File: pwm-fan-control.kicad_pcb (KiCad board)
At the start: 2 copper layers, 29 x 20.5 mm, 20 parts, among them J1 Fan-out, J2 PWM and power, J4 Fan-out, Q1 Q_PMOS_GSD, Q2 Q_PMOS_GSD, U1 LM358

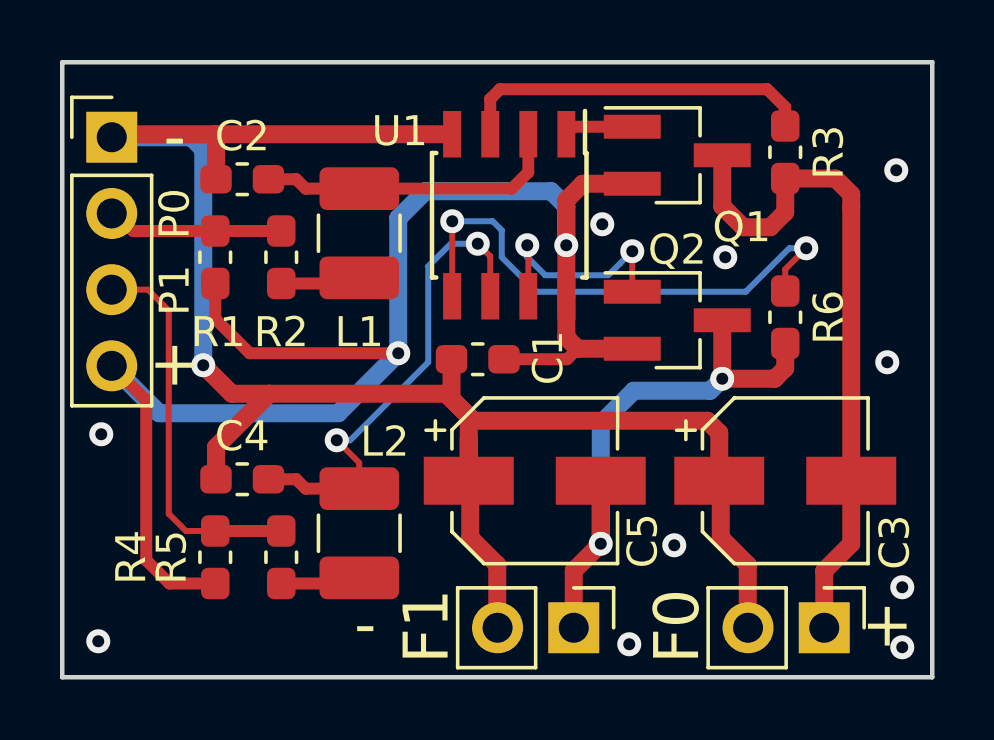
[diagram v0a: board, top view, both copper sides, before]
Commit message: improved bird, added silscreen to the back
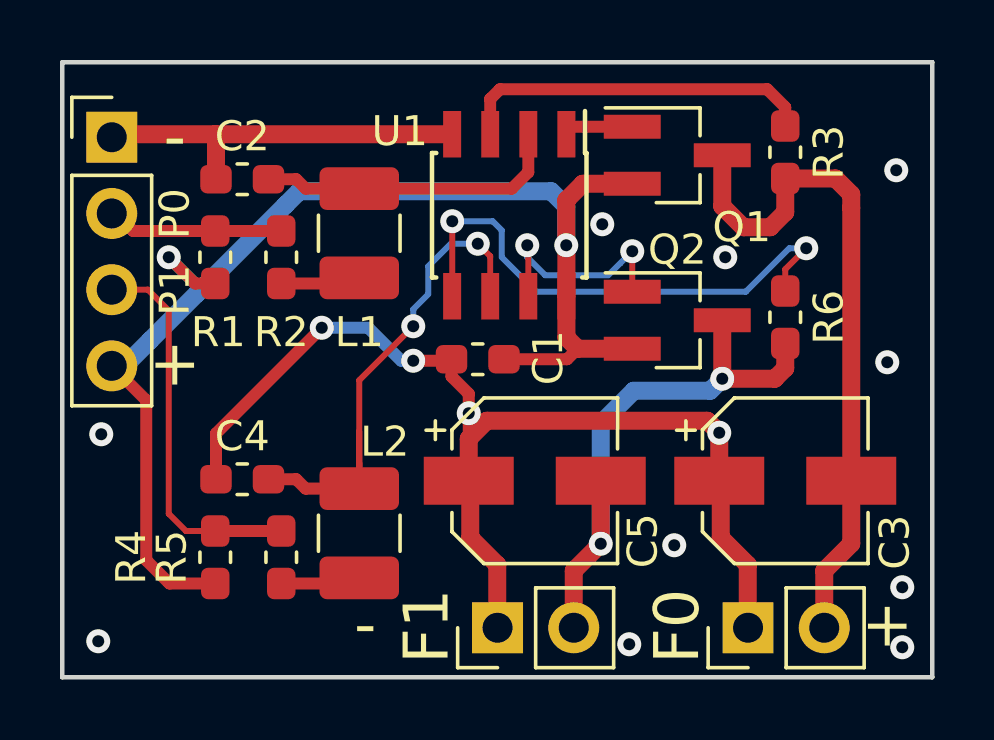
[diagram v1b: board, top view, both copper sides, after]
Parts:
- removed the G*** at (135.7, 56.7)
- added G***: LOGO, graphics:kiwi, B.Cu at (139.0, 55.5)
- moved J4 2.54 mm to (145.5, 58.9), turned to 90 degrees
- moved J1 2.54 mm to (153.9, 58.9), turned to 90 degrees
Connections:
- J1 pad 1: /VFAN0 -> GND
- J1 pad 2: GND -> /VFAN0
- J4 pad 1: /VFAN1 -> GND
- J4 pad 2: GND -> /VFAN1
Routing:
- net GND: track 64.6 -> 50.9 mm, vias 11 -> 14
- net VCCFan: track 54.7 -> 43.4 mm
- net Net-(C4-Pad2): track 16.3 -> 18.2 mm

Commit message: Updated gerbers
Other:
- board text added: "FAN0"
- board text added: "FAN1"
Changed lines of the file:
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@@
   (general
     (thickness 1.6)
-    (drawings 17)
+    (drawings 23)
     (tracks 162)
     (zones 0)
@@
       (xy 1.961326 4.735749) (xy 2.887919 4.58736)) (layer B.Mask) (width 0.01))
   )
+  (gr_text + (at 148 54.4) (layer B.SilkS)
+    (effects (font (size 1.5 1.5) (thickness 0.3)) (justify mirror))
+  )
+  (gr_text + (at 156.4 54.4) (layer B.SilkS)
+    (effects (font (size 1.5 1.5) (thickness 0.3)) (justify mirror))
+  )
+  (gr_text - (at 153.8 54.4) (layer B.SilkS)
+    (effects (font (size 1.5 1.5) (thickness 0.3)) (justify mirror))
+  )
+  (gr_text - (at 145.5 54.4) (layer B.SilkS)
+    (effects (font (size 1.5 1.5) (thickness 0.3)) (justify mirror))
+  )
+  (gr_text FAN0 (at 155 56.2) (layer B.SilkS)
+    (effects (font (size 1.5 1.5) (thickness 0.3)) (justify mirror))
+  )
+  (gr_text FAN1 (at 146.6 56.2) (layer B.SilkS)
+    (effects (font (size 1.5 1.5) (thickness 0.3)) (justify mirror))
+  )
   (gr_text VCCfan (at 134.45 50.15) (layer B.SilkS)

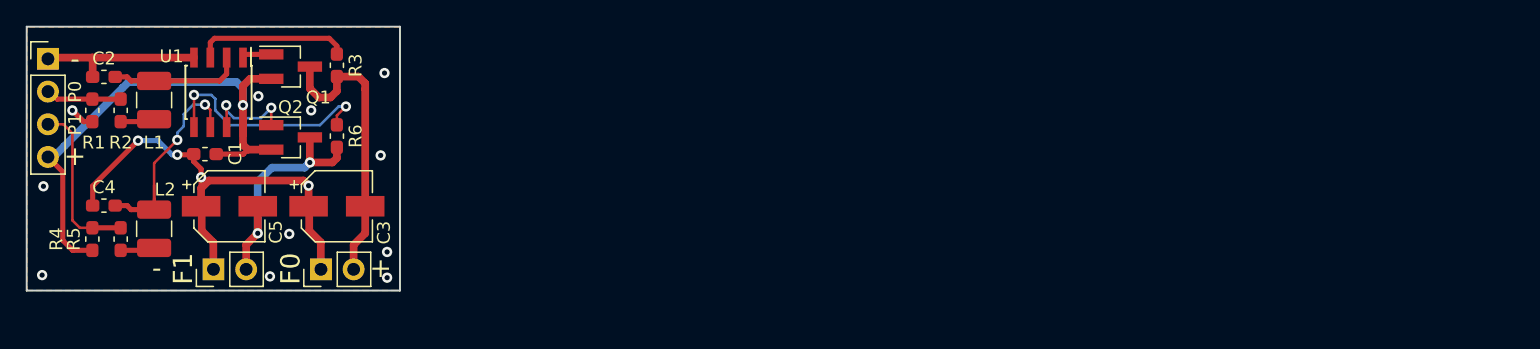
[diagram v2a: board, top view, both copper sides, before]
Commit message: The wizard (N2) came up with a current control scheme instead
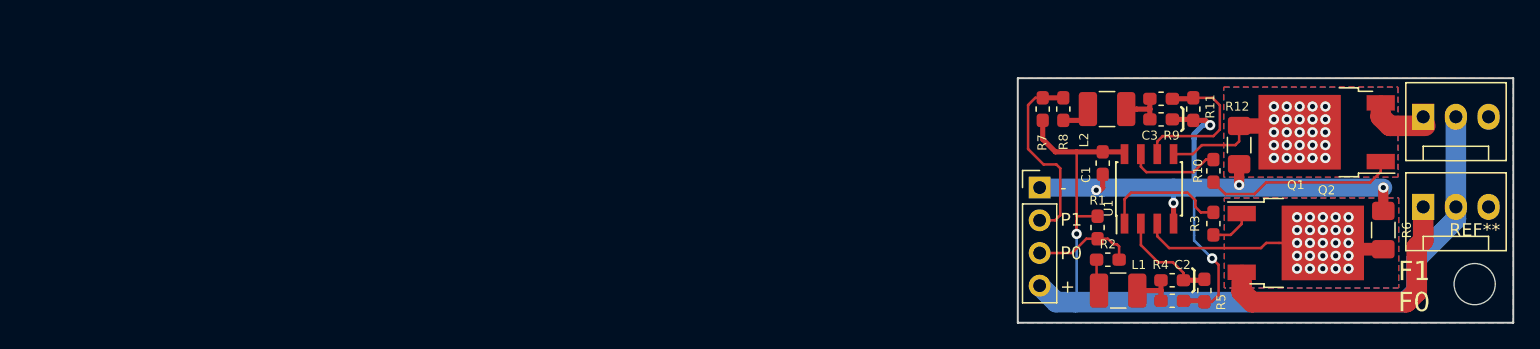
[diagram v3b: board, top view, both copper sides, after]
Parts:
- removed C4: 330nF, Capacitor_SMD:C_0603_1608Metric_Pad1.05x0.95mm_HandSolder
- removed C5: 10uF, Capacitor_SMD:CP_Elec_5x5.4
- removed J4: Fan-out, Connector_PinHeader_2.54mm:PinHeader_1x02_P2.54mm_Vertical
- added J3: Fan-out1, Connector:FanPinHeader_1x03_P2.54mm_Vertical, F.Cu at (239.5, 47.0)
- added R10: 1k, Resistor_SMD:R_0603_1608Metric_Pad1.05x0.95mm_HandSolder, F.Cu at (223.2, 51.2)
- added R11: 47k, Resistor_SMD:R_0603_1608Metric_Pad1.05x0.95mm_HandSolder, F.Cu at (221.6, 46.4)
- added R12: 10R, Resistor_SMD:R_1206_3216Metric_Pad1.42x1.75mm_HandSolder, F.Cu at (225.2, 49.2)
- added R7: 10k, Resistor_SMD:R_0603_1608Metric_Pad1.05x0.95mm_HandSolder, F.Cu at (209.9, 46.4)
- added R8: 220k, Resistor_SMD:R_0603_1608Metric_Pad1.05x0.95mm_HandSolder, F.Cu at (211.5, 46.4)
- added R9: 270k, Resistor_SMD:R_0603_1608Metric_Pad1.05x0.95mm_HandSolder, F.Cu at (219.1, 45.6)
- added REF**: MountingHole_3.2mm_M3, MountingHole:MountingHole_3.2mm_M3, F.Cu at (243.5, 60.0)
- C3: value 10uF -> 330nF; footprint Capacitor_SMD:CP_Elec_5x5.4 -> Capacitor_SMD:C_0603_1608Metric_Pad1.05x0.95mm_HandSolder
- J1: value Fan-out -> Fan-out0; footprint Connector_PinHeader_2.54mm:PinHeader_1x02_P2.54mm_Vertical -> Connector:FanPinHeader_1x03_P2.54mm_Vertical
- L1, L2: value 1mH -> 470uH
- Q1, Q2: value Q_PMOS_GSD -> Q_NMOS_GSD; footprint Package_TO_SOT_SMD:SOT-23_Handsoldering -> Package_TO_SOT_SMD:TO-252-2
- R3: value 10k -> 1k
- R4: value 10k -> 270k
- R5: value 220k -> 47k
- R6: value 10k -> 10R; footprint Resistor_SMD:R_0603_1608Metric_Pad1.05x0.95mm_HandSolder -> Resistor_SMD:R_1206_3216Metric_Pad1.42x1.75mm_HandSolder
- moved J1 85.8 mm to (239.5, 54.0), turned to 0 degrees
- moved C2 84.8 mm to (220.0, 61.3), turned to 180 degrees
- moved R5 84.3 mm to (222.5, 60.5)
- moved R4 84.0 mm to (220.0, 59.7), turned to 180 degrees
- moved R6 81.6 mm to (236.4, 55.8), turned to 270 degrees
- moved Q2 80.5 mm to (232.0, 48.2), turned to 180 degrees
- moved Q1 79.3 mm to (229.6, 56.8)
- moved R1 78.6 mm to (214.2, 55.6), turned to 90 degrees
- moved J2 77.7 mm to (209.7, 52.5)
- moved R2 77.6 mm to (215.0, 58.1), turned to 0 degrees
- moved G*** 77.5 mm to (216.2, 49.5)
- moved L1 76.3 mm to (215.8, 60.5), turned to 0 degrees
- moved L2 74.6 mm to (214.9, 46.4), turned to 0 degrees
- moved U1 72.7 mm to (218.2, 52.6), turned to 90 degrees
- moved C1 69.8 mm to (214.6, 50.6), turned to 90 degrees
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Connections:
- C3 pad 2: /VFAN0 -> Net-(C3-Pad2)
- J1 pad 1: GND -> Net-(J1-Pad1)
- J1 pad 2: /VFAN0 -> VCCFan
- J2 pad 2: /~PWM0 -> /~PWM1
- J2 pad 3: /~PWM1 -> /~PWM0
- L2 pad 2: Net-(C4-Pad2) -> Net-(C3-Pad2)
- Q1 pad 2: VCCFan -> Net-(Q1-Pad2)
- Q1 pad 3: /VFAN0 -> Net-(J1-Pad1)
- Q2 pad 2: VCCFan -> Net-(Q2-Pad2)
- Q2 pad 3: /VFAN1 -> Net-(J3-Pad1)
- R3 pad 1: /VFAN0 -> Net-(Q1-Pad1)
- R4 pad 1: /~PWM1 -> Net-(R4-Pad1)
- R4 pad 2: VCCFan -> Net-(C2-Pad2)
- R5 pad 1: Net-(L2-Pad1) -> GND
- R5 pad 2: /~PWM1 -> Net-(R4-Pad1)
- R6 pad 1: /VFAN1 -> GND
- R6 pad 2: Net-(R6-Pad2) -> Net-(Q1-Pad2)
- U1 pad 1: Net-(Q1-Pad1) -> Net-(R3-Pad2)
- U1 pad 2: Net-(C2-Pad2) -> Net-(R4-Pad1)
- U1 pad 3: Net-(R3-Pad2) -> Net-(Q1-Pad2)
- U1 pad 5: Net-(R6-Pad2) -> Net-(Q2-Pad2)
- U1 pad 6: Net-(C4-Pad2) -> Net-(R11-Pad2)
- U1 pad 7: Net-(Q2-Pad1) -> Net-(R10-Pad2)
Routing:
- net VCCFan: track 43.4 -> 67.6 mm, vias 2 -> 1
- net /VFAN0: track 22.7 -> 0.00 mm
- net Net-(J1-Pad1): track 0.00 -> 22.6 mm
- net /VFAN1: track 19.0 -> 0.00 mm, vias 2 -> 0
- net Net-(Q1-Pad2): track 0.00 -> 18.8 mm, vias 0 -> 25
- net Net-(C4-Pad2): track 18.2 -> 0.00 mm, vias 2 -> 0
- net Net-(R6-Pad2): track 18.1 -> 0.00 mm, vias 2 -> 0
- net Net-(Q2-Pad2): track 0.00 -> 12.3 mm, vias 0 -> 25
- net Net-(R11-Pad2): track 0.00 -> 12.1 mm
- net Net-(R4-Pad1): track 0.00 -> 8.58 mm
- net Net-(Q2-Pad1): track 7.54 -> 14.9 mm, vias 2 -> 0
- net Net-(R10-Pad2): track 0.00 -> 7.19 mm
- net Net-(C2-Pad2): track 10.3 -> 3.54 mm
- net GND: track 50.9 -> 56.1 mm, vias 14 -> 6
- net Net-(J3-Pad1): track 0.00 -> 4.83 mm
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- added copper zone on B.Cu, net Net-(Q1-Pad2)
- added copper zone on F.Cu, net Net-(Q1-Pad2)
- added copper zone on B.Cu, net Net-(Q2-Pad2)
- added copper zone on F.Cu, net Net-(Q2-Pad2)
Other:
- board size 29 x 20.5 mm -> 38.5 x 19 mm
- board text added: "F1 F0"
- board text removed: "F0"
- board text removed: "F1"
- board text removed: "FAN0"
- board text removed: "FAN1"
- board text removed: "GND"
- board text removed: "VCCfan"
- board text removed: "~PWM0"
- board text removed: "~PWM1"

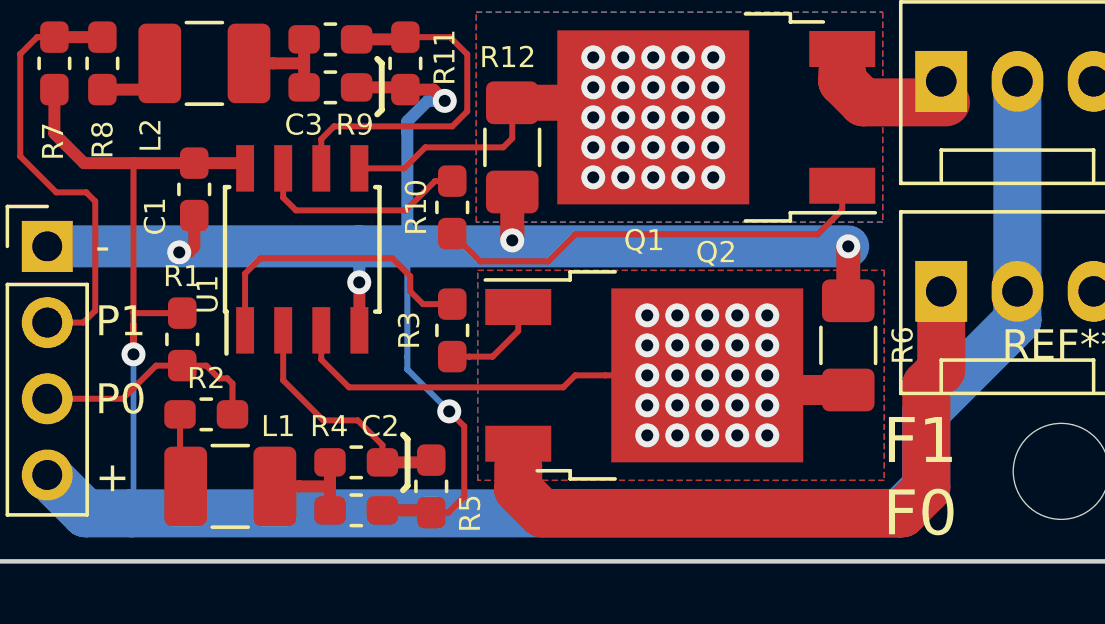
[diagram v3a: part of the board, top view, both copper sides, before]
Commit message: Increased vias on power resistors
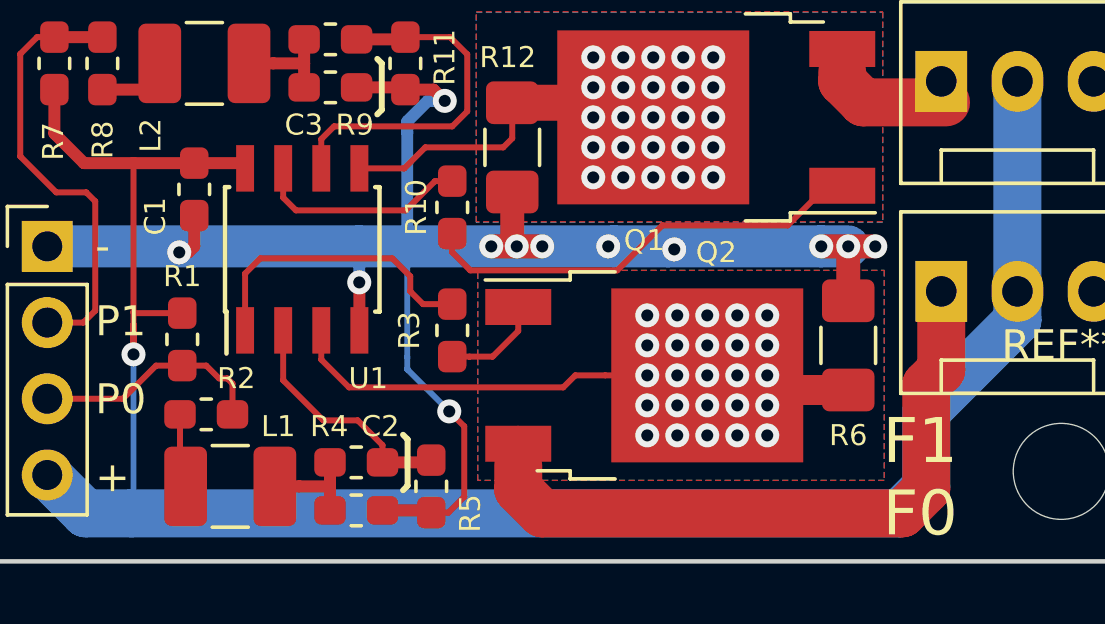
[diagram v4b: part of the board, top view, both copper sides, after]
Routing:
- net GND: track 56.1 -> 59.8 mm, vias 6 -> 12
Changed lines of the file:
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@@
     (thickness 1.6)
     (drawings 20)
-    (tracks 212)
+    (tracks 226)
     (zones 0)
     (modules 25)
@@
     (tags "resistor handsolder")
     (attr smd)
-    (fp_text reference R2 (at 0 -1.2) (layer F.SilkS)
+    (fp_text reference R2 (at 1 -1.2) (layer F.SilkS)
       (effects (font (size 0.7 0.7) (thickness 0.12)))
     )
@@
     (tags "resistor handsolder")
     (attr smd)
-    (fp_text reference R6 (at 0 -1.82 270) (layer F.SilkS)
+    (fp_text reference R6 (at 3 0) (layer F.SilkS)
       (effects (font (size 0.7 0.7) (thickness 0.12)))
     )
@@
     (tags "SOIC 1.27")
     (attr smd)
-    (fp_text reference U1 (at -1.5 -3.15 90) (layer F.SilkS)
+    (fp_text reference U1 (at -4.3 2.2 180) (layer F.SilkS)
       (effects (font (size 0.7 0.7) (thickness 0.12)))
     )
@@
     (effects (font (size 1.5 1.5) (thickness 0.3)))
   )
-  (gr_text git.io/pwm2fan (at 231.4 61.3) (layer B.SilkS)
+  (gr_text git.io/pwm2fan (at 231.4 61.4) (layer B.SilkS)
     (effects (font (size 1.5 1.5) (thickness 0.3)) (justify mirror))
   )
@@
   (segment (start 214.6 51.475) (end 214.6 52.5) (width 0.4) (layer F.Cu) (net 1))
   (segment (start 220.1 52.5) (end 214.6 52.5) (width 1.4) (layer B.Cu) (net 1))
-  (via (at 236.4 52.5) (size 0.8) (drill 0.4) (layers F.Cu B.Cu) (net 1))
-  (segment (start 236.4 54.3125) (end 236.4 52.5) (width 0.8) (layer F.Cu) (net 1))
   (segment (start 214.6 52.5) (end 209.7 52.5) (width 1.4) (layer B.Cu) (net 1))
   (segment (start 223.075 61.375) (end 223.6 60.85) (width 0.2) (layer F.Cu) (net 1))
@@
   (segment (start 220.105 55.3) (end 220.105 53.705) (width 0.4) (layer F.Cu) (net 1))
   (segment (start 220.1 52.5) (end 220.1 53.7) (width 0.4) (layer B.Cu) (net 1))
-  (via (at 225.2 52.3) (size 0.8) (drill 0.4) (layers F.Cu B.Cu) (net 1))
-  (segment (start 225.2 52.3) (end 225.2 50.6875) (width 0.8) (layer F.Cu) (net 1))
-  (segment (start 221.7 52.5) (end 236.4 52.5) (width 1.4) (layer B.Cu) (net 1))
+  (via (at 225.35 52.5) (size 0.8) (drill 0.4) (layers F.Cu B.Cu) (net 1))
+  (segment (start 221.7 52.5) (end 228.6 52.5) (width 1.4) (layer B.Cu) (net 1))
   (via (at 222.95 47.65) (size 0.8) (drill 0.4) (layers F.Cu B.Cu) (net 1))
   (segment (start 221.637895 47.275) (end 222.575 47.275) (width 0.4) (layer F.Cu) (net 1))
@@
   (segment (start 214.4 52.7) (end 214.6 52.5) (width 0.4) (layer F.Cu) (net 1))
   (segment (start 214.1 52.7) (end 214.4 52.7) (width 0.4) (layer F.Cu) (net 1))
+  (via (at 226.2 52.5) (size 0.8) (drill 0.4) (layers F.Cu B.Cu) (net 1))
+  (via (at 224.5 52.5) (size 0.8) (drill 0.4) (layers F.Cu B.Cu) (net 1))
+  (segment (start 236.4 52.5) (end 236.4 52.5) (width 0.6) (layer B.Cu) (net 1))
+  (via (at 236.4 52.5) (size 0.8) (drill 0.4) (layers F.Cu B.Cu) (net 1))
+  (segment (start 235.5 52.5) (end 236.4 52.5) (width 1.4) (layer B.Cu) (net 1))
+  (via (at 235.5 52.5) (size 0.8) (drill 0.4) (layers F.Cu B.Cu) (net 1))
+  (via (at 237.3 52.5) (size 0.8) (drill 0.4) (layers F.Cu B.Cu) (net 1))
+  (segment (start 235.5 52.5) (end 237.3 52.5) (width 0.8) (layer F.Cu) (net 1))
+  (segment (start 236.4 52.5) (end 236.4 54.3125) (width 0.8) (layer F.Cu) (net 1))
+  (segment (start 224.5 52.5) (end 226.2 52.5) (width 0.8) (layer F.Cu) (net 1))
+  (segment (start 225.2 52.35) (end 225.35 52.5) (width 0.8) (layer F.Cu) (net 1))
+  (segment (start 225.2 50.6875) (end 225.2 52.35) (width 0.8) (layer F.Cu) (net 1))
+  (segment (start 230.4 52.5) (end 235.5 52.5) (width 1.4) (layer B.Cu) (net 1))
+  (via (at 230.6 52.6) (size 0.8) (drill 0.4) (layers F.Cu B.Cu) (net 1))
+  (segment (start 228.6 52.5) (end 230.4 52.5) (width 1.4) (layer B.Cu) (net 1))
+  (via (at 228.4 52.5) (size 0.8) (drill 0.4) (layers F.Cu B.Cu) (net 1))
   (segment (start 216.12 49.725) (end 216.295 49.9) (width 0.4) (layer F.Cu) (net 2))
   (segment (start 214.6 49.725) (end 216.12 49.725) (width 0.4) (layer F.Cu) (net 2))
@@
   (segment (start 225.4 55.32) (end 224.545 56.175) (width 0.2) (layer F.Cu) (net 6))
   (segment (start 225.4 54.52) (end 225.4 55.32) (width 0.2) (layer F.Cu) (net 6))
-  (segment (start 224.125 53) (end 223.2 52.075) (width 0.2) (layer F.Cu) (net 7))
-  (segment (start 226.4 53) (end 224.125 53) (width 0.2) (layer F.Cu) (net 7))
-  (segment (start 227.3 52.1) (end 226.4 53) (width 0.2) (layer F.Cu) (net 7))
-  (segment (start 235.38 52.1) (end 227.3 52.1) (width 0.2) (layer F.Cu) (net 7))
-  (segment (start 236.2 50.48) (end 236.2 51.28) (width 0.2) (layer F.Cu) (net 7))
-  (segment (start 236.2 51.28) (end 235.38 52.1) (width 0.2) (layer F.Cu) (net 7))
+  (segment (start 235.7 50.48) (end 236.2 50.48) (width 0.2) (layer F.Cu) (net 7))
+  (segment (start 223.2 52.075) (end 223.2 52.7) (width 0.2) (layer F.Cu) (net 7))
+  (segment (start 223.2 52.7) (end 223.8 53.3) (width 0.2) (layer F.Cu) (net 7))
+  (segment (start 223.8 53.3) (end 228.7 53.3) (width 0.2) (layer F.Cu) (net 7))
+  (segment (start 228.7 53.3) (end 230.2 51.8) (width 0.2) (layer F.Cu) (net 7))
+  (segment (start 230.2 51.8) (end 234.38 51.8) (width 0.2) (layer F.Cu) (net 7))
+  (segment (start 234.38 51.8) (end 235.7 50.48) (width 0.2) (layer F.Cu) (net 7))
   (segment (start 216.295 55.3) (end 216.295 53.405) (width 0.2) (layer F.Cu) (net 8))
   (segment (start 216.295 53.405) (end 216.8 52.9) (width 0.2) (layer F.Cu) (net 8))
@@
   )
   (zone (net 1) (net_name GND) (layer B.Cu) (hatch edge 0.508)
-    (connect_pads yes (clearance 0.3))
+    (connect_pads (clearance 0.3))
     (min_thickness 0.254)
     (fill yes (arc_segments 16) (thermal_gap 0.508) (thermal_bridge_width 0.508))
@@
   )
   (zone (net 1) (net_name GND) (layer F.Cu) (hatch edge 0.508)
-    (connect_pads yes (clearance 0.3))
+    (connect_pads (clearance 0.3))
     (min_thickness 0.254)
     (fill yes (arc_segments 16) (thermal_gap 0.508) (thermal_bridge_width 0.508))
